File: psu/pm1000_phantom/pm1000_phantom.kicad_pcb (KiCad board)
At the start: 2 copper layers, 25 x 42.5 mm, 17 parts, among them J1 2 pin 2,54mm Molex, J10 2 pin 2,54mm Molex, J2 2 pin 2,54mm Molex, J3 2 pin 2,54mm Molex, J4 2 pin 2,54mm Molex, J5 2 pin 2,54mm Molex, J6 3 pin 2,54mm Molex, J7 3 pin 2,54mm Molex, J8 3 pin 2,54mm Molex, J9 3 pin 2,54mm Molex

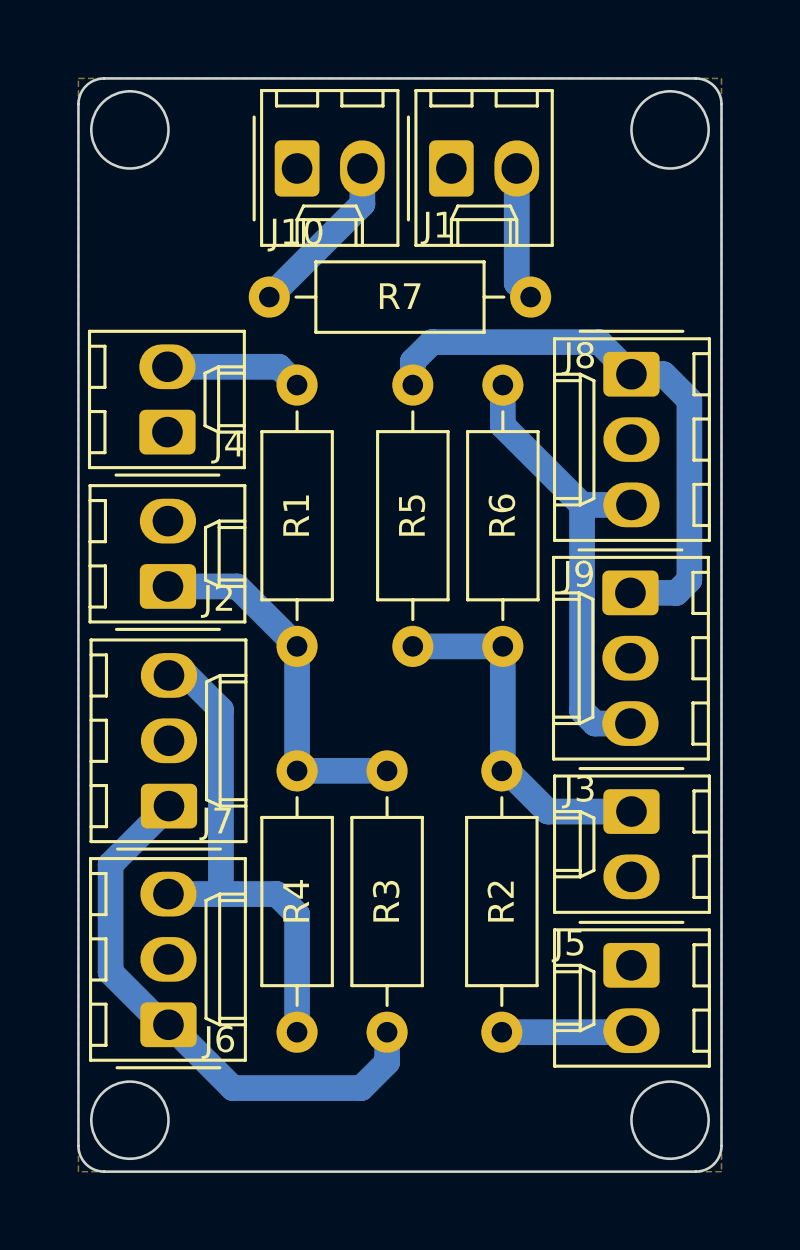
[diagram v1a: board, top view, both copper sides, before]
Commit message: phantom: increase board size, better clearances
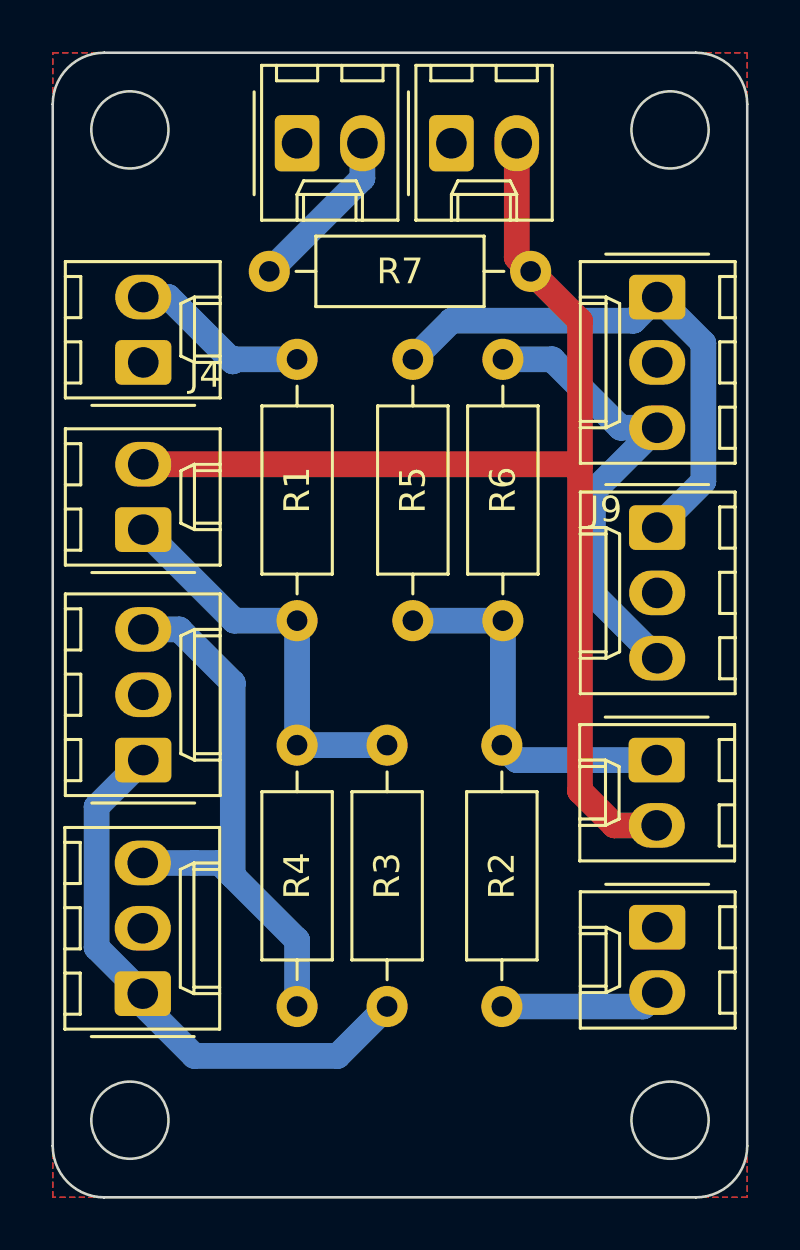
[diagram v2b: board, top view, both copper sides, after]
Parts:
- moved J8 3.16 mm to (82.5, 113.5)
- moved J4 2.87 mm to (62.5, 116.0)
- moved J9 2.74 mm to (82.5, 122.5)
- moved J2 2.41 mm to (62.5, 122.5)
- moved J3 2.23 mm to (82.5, 131.5)
- moved J7 2.05 mm to (62.5, 131.5)
- moved J5 1.79 mm to (82.5, 138.0)
- moved J6 1.57 mm to (62.5, 140.6)
- moved R1 1.00 mm to (68.5, 115.9)
- moved R2 1.00 mm to (76.5, 141.1)
- moved R3 1.00 mm to (72.0, 141.1)
- moved R4 1.00 mm to (68.5, 141.1)
- moved R5 1.00 mm to (73.0, 115.9)
- moved R6 1.00 mm to (76.5, 115.9)
- moved R7 1.00 mm to (77.6, 112.5)
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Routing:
- net +48V: track 5.22 -> 46.7 mm
- net Net-(J6-Pin_3): track 19.6 -> 21.7 mm
- net Net-(J4-Pin_2): track 5.33 -> 7.05 mm
- net +48 switched A: track 14.3 -> 15.8 mm
- net Net-(J8-Pin_1): track 22.4 -> 21.0 mm
- net Net-(J5-Pin_2): track 5.06 -> 6.26 mm
- net +48 switched B: track 14.1 -> 14.6 mm
- net Net-(J6-Pin_1): track 21.6 -> 22.1 mm
- added copper zone on B.Cu, net GND
- removed copper zone on B.Cu, net +48V
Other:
- board size 25 x 42.5 mm -> 27 x 44.5 mm

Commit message: set led resistors to 22k, place new psu terminal block
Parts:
- R1, R2, R7: value 2k2 -> 22k
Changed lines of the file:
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@@
 			)
 		)
-		(property "Value" "2k2"
+		(property "Value" "22k"
 			(at 5.08 2.37 90)
 			(layer "F.Fab")
@@
 			)
 		)
-		(property "Value" "2k2"
+		(property "Value" "22k"
 			(at 5.08 2.37 90)
 			(layer "F.Fab")
@@
 			)
 		)
-		(property "Value" "2k2"
+		(property "Value" "22k"
 			(at 5.08 2.37 0)
 			(layer "F.Fab")
